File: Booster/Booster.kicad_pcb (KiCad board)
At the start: 2 copper layers, 97 x 60 mm, 124 parts, among them IC401 SN754410, J101 Track, J301 15VDC, J601 StatusLED, J701 Conn_01x04, P201 CONN_01X02, P202 CONN_01X02, P601 ~OVERCURRENT_OUT, P602 ~OVERCURRENT_OUT_OP, P603 MSTR_SW, P604 MSTR_SW_OUT, P605 MSTR_SW_OUT_OP, P606 ~DRIVER_ENABLE_OUT_OP, P607 ~DRIVER_ENABLE_OUT, P701 REVERSER_OUT, P702 REVERSER_OUT_OP, Q301 FQP47P06, Q601 BC807-40, Q602 BC807-40, Q603 BC807-40, Q604 BC817-40, Q701 BC817-40, SW601 DIP, U201 6N137, U203 LM339, U301 LM78L05, U501 LM338, U502 LM358, U503 NE555, U504 74HC08, U602 PC817, U603 PC817, U604 PC817, U701 74HC86, U702 PC817

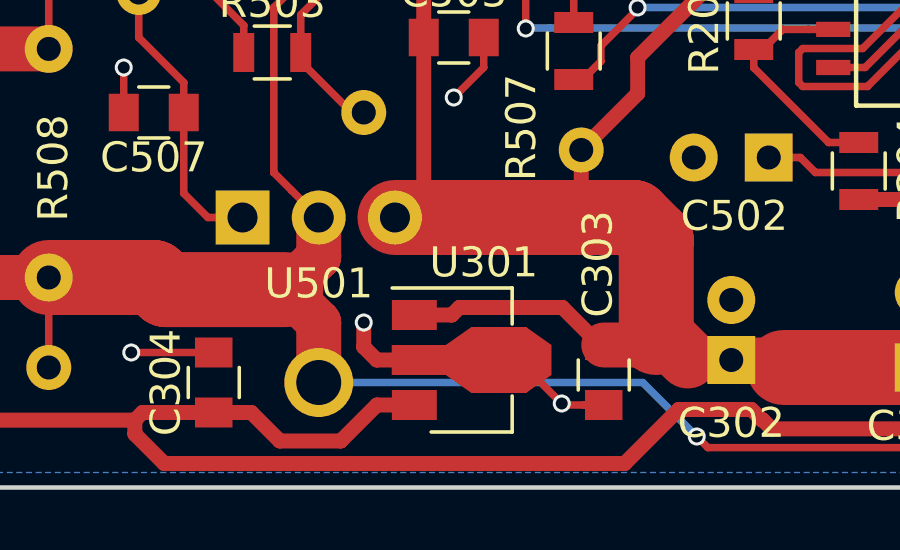
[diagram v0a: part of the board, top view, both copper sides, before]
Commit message: Fixed 7805 ->7805
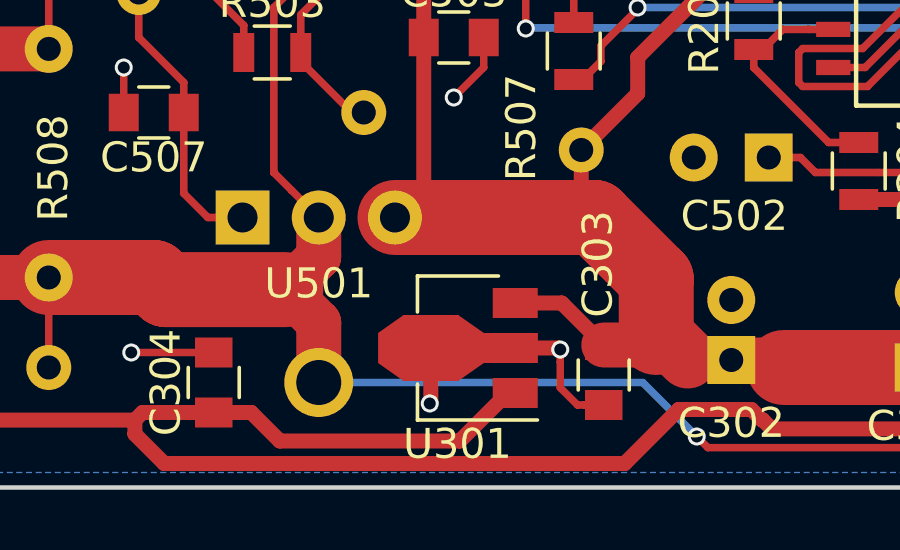
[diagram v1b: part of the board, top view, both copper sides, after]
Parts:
- U301: value LM78L05 -> L78L05_SOT89
- moved U301 0.57 mm to (141.6, 135.3), turned to 180 degrees
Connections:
- U301 pad 1: +15V -> +5V
- U301 pad 3: +5V -> +15V
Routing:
- net +15V: track 62.8 -> 58.7 mm
- net +5V: track 467.7 -> 471.2 mm
- net GND: track 100.9 -> 100.0 mm

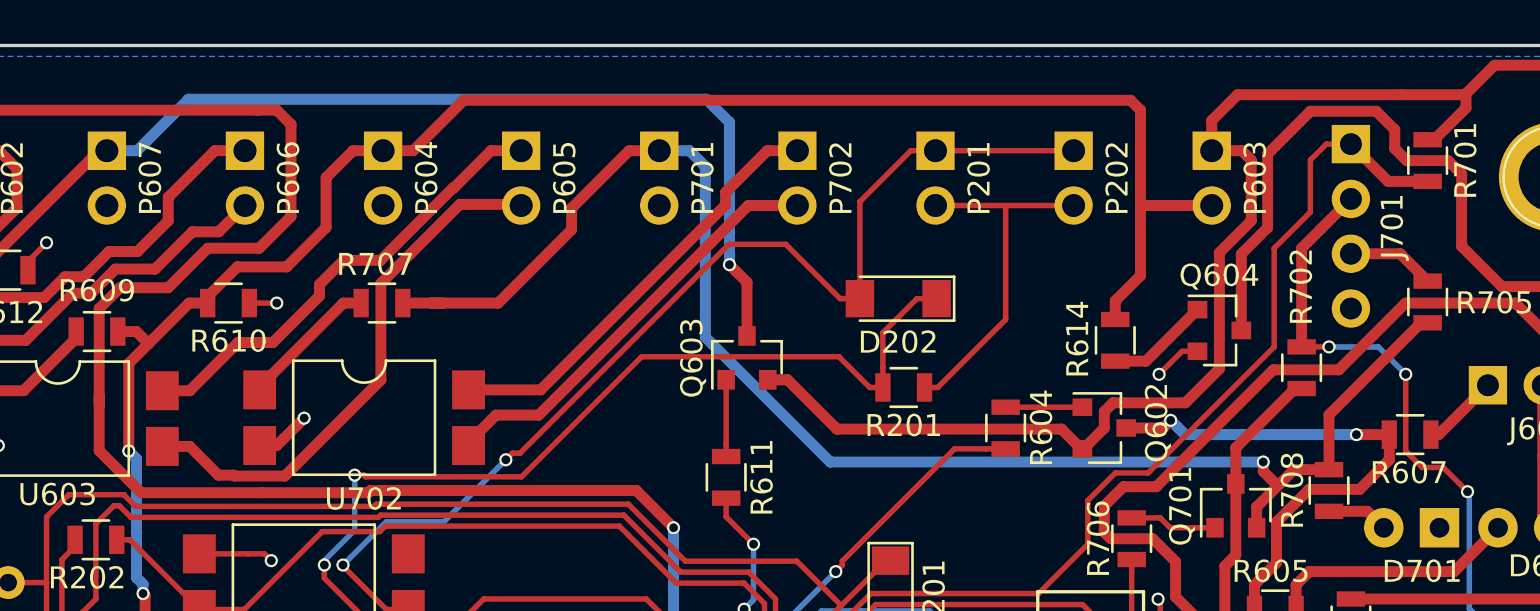
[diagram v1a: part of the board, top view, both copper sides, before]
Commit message: Fixed DCC input direction through optocoupler reversed.
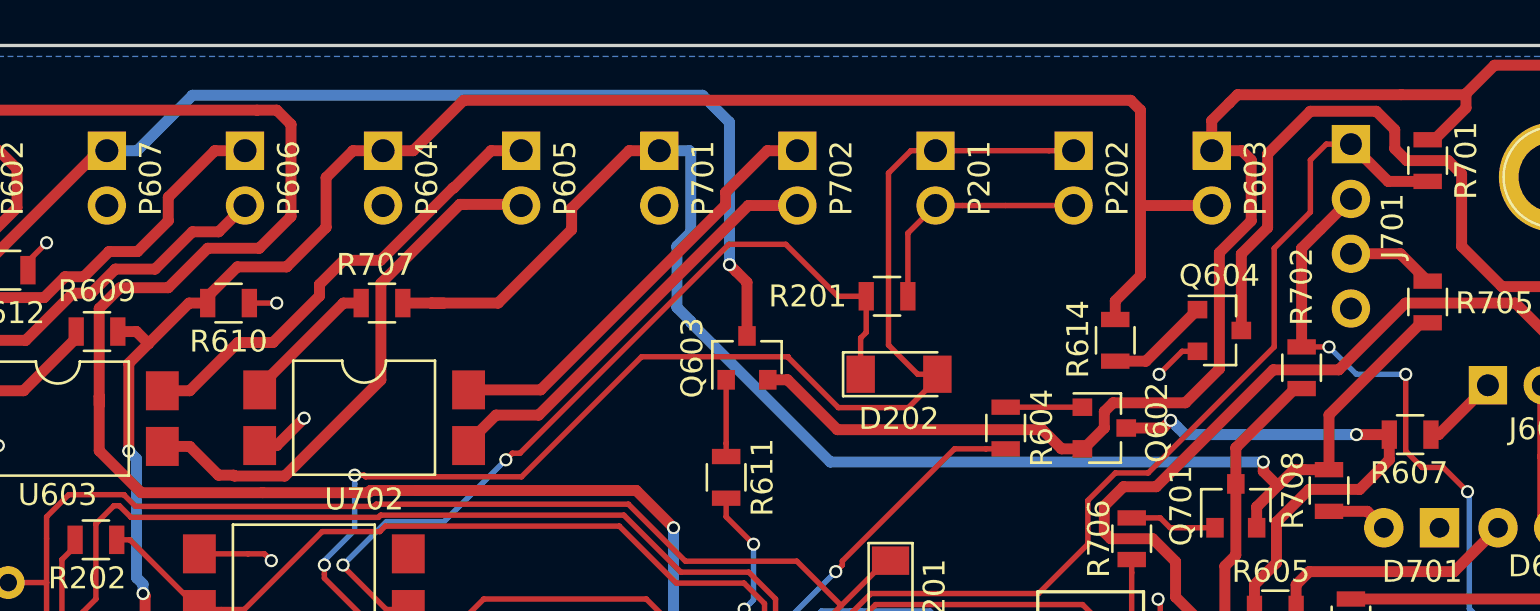
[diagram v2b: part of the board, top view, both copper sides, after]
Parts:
- moved R201 4.23 mm to (160.6, 91.4)
- moved D202 3.45 mm to (161.1, 95.0), turned to 0 degrees
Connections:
- U201 pad 2: Net-(D202-Pad1) -> /DCC Input/DCC_Input
- U201 pad 3: /DCC Input/DCC_Input -> Net-(D202-Pad1)
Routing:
- net /DCC Input/DCC_Input: track 49.7 -> 60.9 mm
- net /DCC Input/DCC_GND_Input: track 16.5 -> 11.2 mm
- net Net-(D202-Pad1): track 43.4 -> 38.4 mm
- net Net-(P701-Pad1): track 69.0 -> 69.5 mm
